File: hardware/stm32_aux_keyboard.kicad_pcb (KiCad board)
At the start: 2 copper layers, 95 x 95 mm, 208 parts, among them J1 I2C_HEADER,2.54, J2 WS2812_HEADER, J3 BUZZER_HEADER, J4 ROT_ENC_HEADER, J5 SWD_SWD, J6 SWD_SWD, J7 ROT_ENC_HEADER, J8 I2C_HEADER,2.54, Q1 SS9013_J3, SW1 USR_BTN_1, SW10 KEY22, SW11 KEY23, SW12 KEY31, SW13 KEY32, SW14 KEY33, SW15 KEY41, SW16 KEY42, SW17 KEY43, SW18 ROT1, SW19 SW_RESET,2_leg,SMD, SW2 USR_BTN_2, SW3 USR_BTN_3, SW4 USR_BTN_4, SW5 ROT2, SW6 KEY11, SW7 KEY12, SW8 KEY13, SW9 KEY21, U1 SSD1306-OLED-I2C, U10 STM32F103C8T6, U2 AMS1117-3.3, U3 74AHCT1G125, U4 USB, U5 USBLC6-2SC6_SOT23-6, U6 STM32F103C8T6_rect, U7 SWD, U8 AMS1117-3.3, U9 USBLC6-2SC6_SOT23-6, Y1 O_8M, Y2 O8M, Y3 O32.768K

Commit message: update route,
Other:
- net class 500mA added: clearance 0.2, trace_width 0.25, via_dia 0.8, via_drill 0.4
- net class 800mA added: clearance 0.4, trace_width 0.25, via_dia 0.8, via_drill 0.4
- net class GND added: clearance 0.2, trace_width 0.25, via_dia 0.8, via_drill 0.4
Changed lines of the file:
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@@
     (uvia_dia 0.3)
     (uvia_drill 0.1)
-    (add_net +3V3)
-    (add_net +5V)
     (add_net /WS2812/WS2812_IN)
     (add_net /keyboard_key/COL1)
@@
     (add_net /stm32_core/OSC_N)
     (add_net /stm32_core/OSC_P)
-    (add_net /stm32_core/PA15)
     (add_net /stm32_core/PC13)
     (add_net /stm32_core/RESET)
     (add_net /stm32_core/ROT_ENC_SW1)
     (add_net /stm32_core/ROT_ENC_SW2)
-    (add_net /stm32_core/TTL_RX)
-    (add_net /stm32_core/TTL_TX)
     (add_net /stm32_core/USB_N)
     (add_net /stm32_core/USB_P)
@@
     (add_net /stm32_swd/USB_N)
     (add_net /stm32_swd/USB_P)
-    (add_net GND)
     (add_net "Net-(BZ1-PadN)")
     (add_net "Net-(C29-Pad2)")
     (add_net "Net-(C30-Pad2)")
     (add_net "Net-(C32-Pad1)")
-    (add_net "Net-(C52-Pad1)")
-    (add_net "Net-(C52-Pad2)")
-    (add_net "Net-(C53-Pad1)")
-    (add_net "Net-(C53-Pad2)")
-    (add_net "Net-(C54-Pad1)")
-    (add_net "Net-(C54-Pad2)")
-    (add_net "Net-(C55-Pad1)")
-    (add_net "Net-(C55-Pad2)")
-    (add_net "Net-(C56-Pad1)")
-    (add_net "Net-(C56-Pad2)")
-    (add_net "Net-(C57-Pad1)")
-    (add_net "Net-(C57-Pad2)")
-    (add_net "Net-(C58-Pad1)")
-    (add_net "Net-(C58-Pad2)")
-    (add_net "Net-(C59-Pad1)")
-    (add_net "Net-(C59-Pad2)")
     (add_net "Net-(D1-Pad1)")
     (add_net "Net-(D10-Pad2)")
@@
     (add_net "Net-(D21-Pad2)")
     (add_net "Net-(D22-Pad2)")
-    (add_net "Net-(D23-Pad2)")
     (add_net "Net-(D25-Pad1)")
     (add_net "Net-(D26-Pad2)")
@@
     (add_net "Net-(R3-Pad2)")
     (add_net "Net-(R30-Pad1)")
-    (add_net "Net-(R37-Pad1)")
-    (add_net "Net-(R37-Pad2)")
-    (add_net "Net-(R38-Pad1)")
-    (add_net "Net-(R38-Pad2)")
-    (add_net "Net-(R39-Pad1)")
-    (add_net "Net-(R39-Pad2)")
-    (add_net "Net-(R40-Pad1)")
-    (add_net "Net-(R40-Pad2)")
     (add_net "Net-(RN1-Pad1)")
     (add_net "Net-(RN1-Pad2)")
-    (add_net "Net-(RN1-Pad3)")
-    (add_net "Net-(RN1-Pad4)")
-    (add_net "Net-(RN1-Pad5)")
-    (add_net "Net-(RN1-Pad6)")
-    (add_net "Net-(RN2-Pad3)")
-    (add_net "Net-(RN2-Pad4)")
-    (add_net "Net-(RN2-Pad5)")
-    (add_net "Net-(RN2-Pad6)")
     (add_net "Net-(RN2-Pad7)")
-    (add_net "Net-(RN3-Pad3)")
-    (add_net "Net-(RN3-Pad4)")
-    (add_net "Net-(RN3-Pad5)")
-    (add_net "Net-(RN3-Pad6)")
     (add_net "Net-(RN4-Pad1)")
-    (add_net "Net-(RN4-Pad3)")
-    (add_net "Net-(RN4-Pad4)")
-    (add_net "Net-(RN4-Pad5)")
-    (add_net "Net-(RN4-Pad6)")
     (add_net "Net-(U4-Pad2)")
     (add_net "Net-(U4-Pad3)")
-    (add_net "Net-(U6-Pad11)")
-    (add_net "Net-(U6-Pad12)")
-    (add_net "Net-(U6-Pad13)")
-    (add_net "Net-(U6-Pad14)")
-    (add_net "Net-(U6-Pad15)")
-    (add_net "Net-(U6-Pad16)")
-    (add_net "Net-(U6-Pad17)")
-    (add_net "Net-(U6-Pad18)")
-    (add_net "Net-(U6-Pad19)")
-    (add_net "Net-(U6-Pad21)")
-    (add_net "Net-(U6-Pad22)")
-    (add_net "Net-(U6-Pad28)")
-    (add_net "Net-(U6-Pad29)")
-    (add_net "Net-(U6-Pad3)")
-    (add_net "Net-(U6-Pad31)")
-    (add_net "Net-(U6-Pad38)")
-    (add_net "Net-(U6-Pad39)")
-    (add_net "Net-(U6-Pad4)")
-    (add_net "Net-(U6-Pad40)")
-    (add_net "Net-(U6-Pad41)")
-    (add_net "Net-(U6-Pad42)")
-    (add_net "Net-(U6-Pad43)")
-    (add_net "Net-(U6-Pad45)")
-    (add_net "Net-(U6-Pad46)")
     (add_net "Net-(U7-Pad2)")
     (add_net "Net-(U7-Pad3)")
+  )
+  (net_class 500mA ""
+    (clearance 0.2)
+    (trace_width 0.25)
+    (via_dia 0.8)
+    (via_drill 0.4)
+    (uvia_dia 0.3)
+    (uvia_drill 0.1)
+    (add_net +5V)
+  )
+  (net_class 800mA ""
+    (clearance 0.4)
+    (trace_width 0.25)
+    (via_dia 0.8)
+    (via_drill 0.4)
+    (uvia_dia 0.3)
+    (uvia_drill 0.1)
+    (add_net +3V3)
     (add_net VCC)
     (add_net Vbuzzer)
@@
     (add_net Vusb_1)
   )
+  (net_class GND ""
+    (clearance 0.2)
+    (trace_width 0.25)
+    (via_dia 0.8)
+    (via_drill 0.4)
+    (uvia_dia 0.3)
+    (uvia_drill 0.1)
+    (add_net GND)
+  )
   (module footprint-lib:I2C_DEBUG,2.54 (layer F.Cu)

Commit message: update route,
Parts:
- removed C10, C11, C12, C13, C14, C15, C16, C17, C18, C19, C20, C21, C22, C23, C24, C7, C8, C9: C106,0805, Capacitor_SMD:C_0805_2012Metric_Pad1.15x1.40mm_HandSolder
- removed C5, C6: C106,0603, Capacitor_SMD:C_0603_1608Metric_Pad1.05x0.95mm_HandSolder
- removed D10, D11, D12, D13, D14, D15, D16, D17, D18, D19, D20, D21, D22, D23, D6, D7, D8, D9: WS2812B, LED_SMD:LED_WS2812B_PLCC4_5.0x5.0mm_P3.2mm
- removed D3: USR_LED_1, footprint-lib:LED_0603_1608Metric
- removed D36, D37, D38: D_1N4148_T4, Diode_SMD:D_SOD-123
- removed D4: USR_LED_2, footprint-lib:LED_0603_1608Metric
- removed D5: USR_LED_3, footprint-lib:LED_0603_1608Metric
- removed J2: WS2812_HEADER, Connector_PinHeader_1.27mm:PinHeader_1x02_P1.27mm_Vertical
- removed R7, R8, R9: R103,0603, Resistor_SMD:R_0603_1608Metric_Pad1.05x0.95mm_HandSolder
- removed SW15: KEY41, footprint-lib:cherry_mx_without_led_100H
- removed SW16: KEY42, footprint-lib:cherry_mx_without_led_100H
- removed SW17: KEY43, footprint-lib:cherry_mx_without_led_100H
- removed U3: 74AHCT1G125, Package_TO_SOT_SMD:SOT-23-5_HandSoldering
- C25, C26, C27, C28, C29, C30, C31, C32, C33, C34, C35, C39, C40, C41, C42, C43, C44, C45, C46, C47, C48, C49, C50, C51, C52, C53, C54, C55, C56, C57, C58, C59, D24, D25, D26, D27, D28, D29, D30, D31, D32, D33, D34, D35, J7, JP7, JP8, Q1, R10, R11, R12, R13, R14, R15, R16, R17, R18, R19, R20, R21, R24, R25, R28, R29, R30, R33, R37, R38, R39, R40, RN3, U5, VUSB1_HEALTHY1: moved to B.Cu
- D1, D2, D39: footprint LED_SMD:LED_0805_2012Metric_Pad1.15x1.40mm_HandSolder -> footprint-lib:LED_0603_1608Metric
- U2: value AMS1117-3.3 -> footprint-lib:AMS1117_SOT-223; footprint Package_TO_SOT_SMD:SOT-223-3_TabPin2 -> footprint-lib:AMS1117_SOT-223
- U8: footprint Package_TO_SOT_SMD:SOT-223-3_TabPin2 -> footprint-lib:AMS1117_SOT-223
- moved R10 300.0 mm to (26.0, 33.0), turned to 180 degrees
- moved SW1 300.0 mm to (26.0, 33.0)
- moved SW2 297.5 mm to (26.0, 38.0)
- moved R11 294.5 mm to (26.0, 38.0), turned to 180 degrees
- moved R30 289.9 mm to (53.5, 107.0)
- moved C41 289.5 mm to (53.5, 102.0), turned to 180 degrees
- moved R12 289.0 mm to (26.0, 43.0), turned to 180 degrees
- moved SW3 287.0 mm to (26.0, 43.0)
- moved C53 286.1 mm to (24.0, 87.0), turned to 90 degrees
- moved SW4 284.8 mm to (26.0, 48.0)
- moved R13 283.6 mm to (26.0, 48.0), turned to 180 degrees
- moved R39 282.1 mm to (26.0, 53.0), turned to 90 degrees
- moved R28 281.8 mm to (61.5, 102.5), turned to 180 degrees
- moved R38 278.6 mm to (24.0, 77.0), turned to 90 degrees
- moved C39 277.5 mm to (61.5, 106.5)
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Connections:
- net VCC renamed Vws2812
- J1 pad SCL: /oled/SCL -> /SCL
- J1 pad SDA: /oled/SDA -> /SDA
- R1 pad 2: /oled/SCL -> /SCL
- R2 pad 2: /oled/SDA -> /SDA
- U1 pad SCL: /oled/SCL -> /SCL
- U1 pad SDA: /oled/SDA -> /SDA
- U10 pad 14: /keyboard_key/ROW4 -> (no net)
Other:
- net class 500mA removed
- net class 800mA removed
- net class GND removed
- rule pad_to_mask_clearance: 0.051 -> 0

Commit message: update for routing,
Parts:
- removed R13: R103,0603, Resistor_SMD:R_0603_1608Metric_Pad1.05x0.95mm_HandSolder
- removed SW4: USR_BTN_4, footprint-lib:SW_SPST_CK_RS282G05A3
- C38, C4, R3, R4, U8: moved to B.Cu
- U2: value footprint-lib:AMS1117_SOT-223 -> AMS1117-3.3; moved to B.Cu
- VUSB1_HEALTHY1: moved to F.Cu
- moved R10 79.9 mm to (70.2, 99.6)
- moved R11 79.9 mm to (70.2, 104.6)
- moved R12 79.9 mm to (70.2, 109.6)
- moved SW1 79.9 mm to (70.2, 99.6)
- moved SW2 79.9 mm to (70.2, 104.6)
- moved SW3 79.9 mm to (70.2, 109.6)
- moved R15 35.2 mm to (81.6, 110.5)
- moved BZ1 35.2 mm to (81.5, 107.0)
- moved D24 35.2 mm to (78.5, 107.5)
- moved J3 35.2 mm to (81.0, 100.5)
- moved Q1 35.2 mm to (81.5, 107.5)
- moved C25 35.2 mm to (84.5, 107.5)
- moved F1 19.0 mm to (98.8, 86.5), turned to 0 degrees
- moved D1 18.3 mm to (89.8, 83.5), turned to 0 degrees
- moved U2 18.1 mm to (96.2, 84.0)
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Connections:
- net Vws2812 renamed VCC
- C42 pad 1: +3V3 -> Vstm32
- J1 pad SCL: /SCL -> /oled/SCL
- J1 pad SDA: /SDA -> /oled/SDA
- R1 pad 2: /SCL -> /oled/SCL
- R2 pad 2: /SDA -> /oled/SDA
- U1 pad SCL: /SCL -> /oled/SCL
- U1 pad SDA: /SDA -> /oled/SDA
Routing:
- net GND: track 0.00 -> 589.7 mm, vias 0 -> 6
- net Vstm32_stlink: track 0.00 -> 161.5 mm, vias 0 -> 1
- net /stm32_core/ROT_ENC_SW1: track 0.00 -> 148.3 mm
- net /keyboard_key/COL1: track 0.00 -> 139.3 mm, vias 0 -> 4
- net /keyboard_key/ROW2: track 0.00 -> 131.5 mm, vias 0 -> 1
- net /keyboard_key/ROW3: track 0.00 -> 123.9 mm, vias 0 -> 1
- net /keyboard_key/COL2: track 0.00 -> 116.8 mm
- net /stm32_core/ROT_ENC_SW2: track 0.00 -> 113.3 mm, vias 0 -> 1
- net /rot_enc/B: track 0.00 -> 111.6 mm, vias 0 -> 3
- net Vstm32: track 0.00 -> 106.0 mm, vias 0 -> 2
- net /rot_enc2/B: track 0.00 -> 106.0 mm
- net /rot_enc/A: track 0.00 -> 103.5 mm, vias 0 -> 1
- net /oled/SCL: track 0.00 -> 102.5 mm
- net /stm32_core/USR_BTN3: track 0.00 -> 101.5 mm, vias 0 -> 2
- net /rot_enc2/A: track 0.00 -> 101.1 mm
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
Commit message: update ws2812,
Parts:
- added C10: C106,0805, Capacitor_SMD:C_0805_2012Metric_Pad1.15x1.40mm_HandSolder, F.Cu at (190.8, 106.8)
- added C11: C106,0805, Capacitor_SMD:C_0805_2012Metric_Pad1.15x1.40mm_HandSolder, F.Cu at (182.3, 115.4)
- added C12: C106,0805, Capacitor_SMD:C_0805_2012Metric_Pad1.15x1.40mm_HandSolder, F.Cu at (176.1, 119.1)
- added C13: C106,0805, Capacitor_SMD:C_0805_2012Metric_Pad1.15x1.40mm_HandSolder, F.Cu at (190.8, 103.9)
- added C14: C106,0805, Capacitor_SMD:C_0805_2012Metric_Pad1.15x1.40mm_HandSolder, F.Cu at (182.3, 112.5)
- added C15: C106,0805, Capacitor_SMD:C_0805_2012Metric_Pad1.15x1.40mm_HandSolder, F.Cu at (171.3, 119.1)
- added C16: C106,0805, Capacitor_SMD:C_0805_2012Metric_Pad1.15x1.40mm_HandSolder, F.Cu at (166.6, 119.1)
- added C17: C106,0805, Capacitor_SMD:C_0805_2012Metric_Pad1.15x1.40mm_HandSolder, F.Cu at (161.8, 119.1)
- added C5: C106,0603, Capacitor_SMD:C_0603_1608Metric_Pad1.05x0.95mm_HandSolder, F.Cu at (202.0, 99.0)
- added C6: C106,0603, Capacitor_SMD:C_0603_1608Metric_Pad1.05x0.95mm_HandSolder, F.Cu at (190.6, 109.5)
- added C7: C106,0805, Capacitor_SMD:C_0805_2012Metric_Pad1.15x1.40mm_HandSolder, F.Cu at (157.1, 119.1)
- added C8: C106,0805, Capacitor_SMD:C_0805_2012Metric_Pad1.15x1.40mm_HandSolder, F.Cu at (180.8, 119.1)
- added C9: C106,0805, Capacitor_SMD:C_0805_2012Metric_Pad1.15x1.40mm_HandSolder, F.Cu at (187.1, 112.5)
- added D10: WS2812B, footprint-lib:LED_WS2812B_5050_white, F.Cu at (57.5, 56.0)
- added D11: WS2812B, footprint-lib:LED_WS2812B_5050_white, F.Cu at (77.5, 56.0)
- added D12: WS2812B, footprint-lib:LED_WS2812B_5050_white, F.Cu at (37.5, 75.5)
- added D13: WS2812B, footprint-lib:LED_WS2812B_5050_white, F.Cu at (57.5, 75.5)
- added D14: WS2812B, footprint-lib:LED_WS2812B_5050_white, F.Cu at (77.5, 75.5)
- added D15: WS2812B, footprint-lib:LED_WS2812B_5050_white, F.Cu at (93.8, 108.3)
- added D16: WS2812B, footprint-lib:LED_WS2812B_5050_white, F.Cu at (93.8, 99.6)
- added D3: USR_LED_1, footprint-lib:LED_0603_1608Metric, F.Cu at (206.2, 104.1)
- added D4: USR_LED_2, footprint-lib:LED_0603_1608Metric, F.Cu at (210.6, 99.0)
- added D5: USR_LED_3, footprint-lib:LED_0603_1608Metric, F.Cu at (206.2, 101.5)
- added D6: WS2812B, footprint-lib:LED_WS2812B_5050_white, F.Cu at (37.5, 36.5)
- added D7: WS2812B, footprint-lib:LED_WS2812B_5050_white, F.Cu at (57.5, 36.5)
- added D8: WS2812B, footprint-lib:LED_WS2812B_5050_white, F.Cu at (77.5, 36.5)
- added D9: WS2812B, footprint-lib:LED_WS2812B_5050_white, F.Cu at (37.5, 56.0)
- added J2: WS2812_HEADER, Connector_PinHeader_1.27mm:PinHeader_1x02_P1.27mm_Vertical, F.Cu at (186.8, 115.6)
- added R13: R103,0603, Resistor_SMD:R_0603_1608Metric_Pad1.05x0.95mm_HandSolder, F.Cu at (156.9, 130.8)
- added R7: R103,0603, Resistor_SMD:R_0603_1608Metric_Pad1.05x0.95mm_HandSolder, F.Cu at (202.0, 104.0)
- added R8: R103,0603, Resistor_SMD:R_0603_1608Metric_Pad1.05x0.95mm_HandSolder, F.Cu at (206.3, 99.0)
- added R9: R103,0603, Resistor_SMD:R_0603_1608Metric_Pad1.05x0.95mm_HandSolder, F.Cu at (202.0, 101.5)
- added SW4: USR_BTN_4, footprint-lib:SW_SPST_CK_RS282G05A3, F.Cu at (160.1, 127.0)
- added U3: 74AHCT1G125, Package_TO_SOT_SMD:SOT-23-5_HandSoldering, F.Cu at (191.3, 100.1)
- D25, D26, R25, RN3: moved to F.Cu
- D39, R22, R23, R34: moved to B.Cu
- moved U9 144.3 mm to (182.8, 126.5), turned to 0 degrees
- moved R27 143.9 mm to (178.5, 125.7), turned to 0 degrees
- moved R26 143.3 mm to (174.4, 130.5), turned to 0 degrees
- moved RN4 142.4 mm to (174.3, 126.8), turned to 0 degrees
- moved F1 74.6 mm to (59.0, 23.4), turned to 90 degrees
- moved R4 73.9 mm to (67.5, 26.6), turned to 270 degrees
- moved C2 73.2 mm to (65.5, 26.4), turned to 270 degrees
- moved R3 71.8 mm to (63.2, 26.6), turned to 90 degrees
- moved U2 70.4 mm to (56.5, 25.9), turned to 270 degrees
- moved C3 69.6 mm to (52.5, 25.9), turned to 90 degrees
- moved C4 69.4 mm to (51.0, 25.9), turned to 90 degrees
- moved R23 69.0 mm to (106.5, 31.9), turned to 90 degrees
- moved R22 66.3 mm to (104.0, 31.9), turned to 90 degrees
- moved JP5 59.9 mm to (105.2, 32.0), turned to 90 degrees
- moved D2 59.1 mm to (79.0, 29.9), turned to 90 degrees
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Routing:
- net GND: track 589.7 -> 94.7 mm, vias 6 -> 0
- net /stm32_core/ROT_ENC_SW1: track 148.3 -> 0.00 mm
- net /keyboard_key/COL1: track 139.3 -> 0.00 mm, vias 4 -> 0
- net /keyboard_key/ROW2: track 131.5 -> 0.00 mm, vias 1 -> 0
- net /keyboard_key/ROW3: track 123.9 -> 0.00 mm, vias 1 -> 0
- net /keyboard_key/COL2: track 116.8 -> 0.00 mm
- net /stm32_core/ROT_ENC_SW2: track 113.3 -> 0.00 mm, vias 1 -> 0
- net /rot_enc/B: track 111.6 -> 0.00 mm, vias 3 -> 0
- net Vstm32: track 106.0 -> 0.00 mm, vias 2 -> 0
- net /rot_enc2/B: track 106.0 -> 0.00 mm
- net /rot_enc/A: track 103.5 -> 0.00 mm, vias 1 -> 0
- net /oled/SCL: track 102.5 -> 0.00 mm
- net /stm32_core/USR_BTN3: track 101.5 -> 0.00 mm, vias 2 -> 0
- net /rot_enc2/A: track 101.1 -> 0.00 mm
- net /keyboard_key/ROW1: track 98.8 -> 0.00 mm, vias 1 -> 0
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
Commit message: update remote btn4 and all capacitor in place,
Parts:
- removed R13: R103,0603, Resistor_SMD:R_0603_1608Metric_Pad1.05x0.95mm_HandSolder
- removed SW4: USR_BTN_4, footprint-lib:SW_SPST_CK_RS282G05A3
- C10, C11, C12, C13, C14, C15, C16, C17, C7, C8, C9: moved to B.Cu
- moved C10 161.3 mm to (37.7, 56.0), turned to 90 degrees
- moved C13 155.6 mm to (37.8, 75.5), turned to 90 degrees
- moved C8 148.4 mm to (57.3, 36.8), turned to 90 degrees
- moved C7 145.3 mm to (37.5, 36.5), turned to 90 degrees
- moved C11 138.0 mm to (57.7, 56.1), turned to 90 degrees
- moved C9 133.5 mm to (77.5, 36.3), turned to 90 degrees
- moved C14 130.0 mm to (57.8, 75.3), turned to 90 degrees
- moved C12 116.7 mm to (77.9, 56.0), turned to 90 degrees
- moved C15 103.5 mm to (77.5, 75.4), turned to 90 degrees
- moved C16 73.6 mm to (93.8, 108.3), turned to 90 degrees
- moved C17 70.7 mm to (93.8, 99.6), turned to 90 degrees

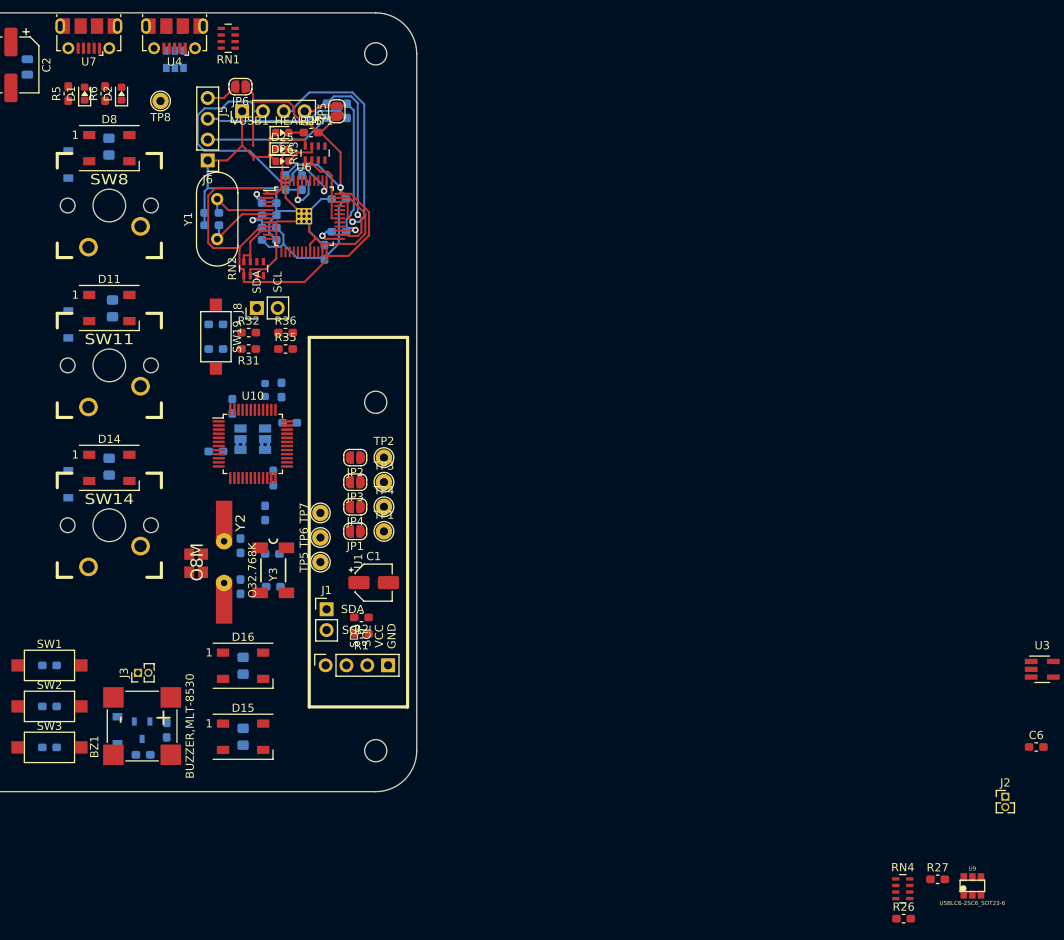
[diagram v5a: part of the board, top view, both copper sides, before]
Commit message: update remote btn4 and all capacitor in place,
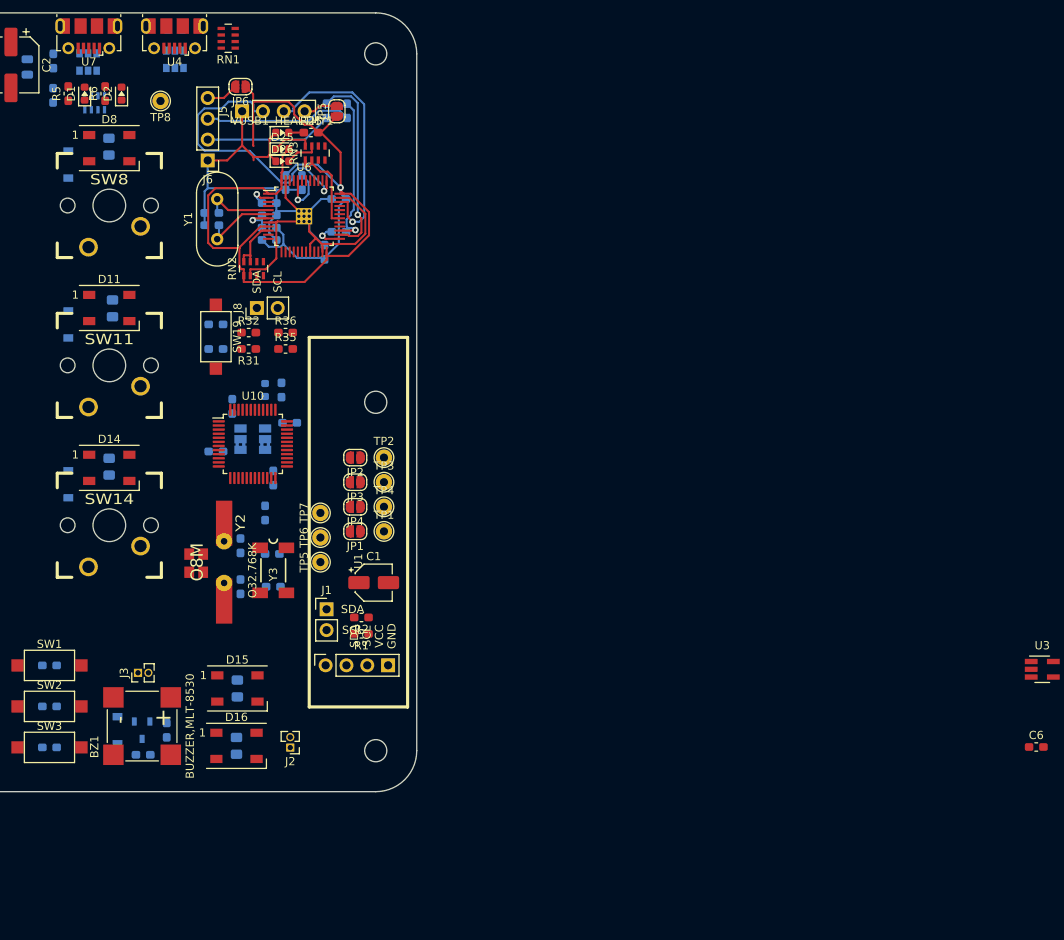
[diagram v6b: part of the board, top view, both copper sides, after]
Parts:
- R26, R27, RN4, U9: moved to B.Cu
- moved U9 147.4 mm to (74.9, 26.0)
- moved R26 147.3 mm to (70.7, 25.9), turned to 90 degrees
- moved R27 144.2 mm to (70.6, 30.1), turned to 90 degrees
- moved RN4 137.5 mm to (75.7, 31.0), turned to 90 degrees
- moved J2 87.4 mm to (99.6, 109.6), turned to 180 degrees
- moved C17 9.80 mm to (93.0, 109.4)
- moved D16 9.80 mm to (93.0, 109.4)
- moved C16 5.93 mm to (93.1, 102.4)
- moved D15 5.93 mm to (93.1, 102.4)

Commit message: update for place complete,
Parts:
- R7, R8, R9: moved to B.Cu
- moved D4 194.3 mm to (23.9, 45.0)
- moved D3 192.4 mm to (24.0, 42.3)
- moved R8 190.4 mm to (23.8, 45.0)
- moved D5 189.8 mm to (24.1, 48.1)
- moved R7 188.4 mm to (24.0, 42.2)
- moved R9 185.8 mm to (24.0, 48.2)
- moved C5 184.6 mm to (24.0, 50.1)
- moved C6 180.7 mm to (24.5, 38.3)
- moved U3 178.8 mm to (24.8, 34.9)

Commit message: update for add supporting hold,
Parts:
- added H7: MOUNT_M2, footprint-lib:MountingHole_2.7mm_M2.5,rpi_like, F.Cu at (67.5, 72.5)
- added H8: MOUNT_M2, footprint-lib:MountingHole_2.7mm_M2.5,rpi_like, F.Cu at (47.5, 52.5)
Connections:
- U10 pad 40: /stm32_core/USR_BTN4 -> (no net)
